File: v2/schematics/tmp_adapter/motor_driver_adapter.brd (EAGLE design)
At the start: 11.8 x 20.2 mm, 2 parts, among them IC1 L293D, IC2 DRV8835

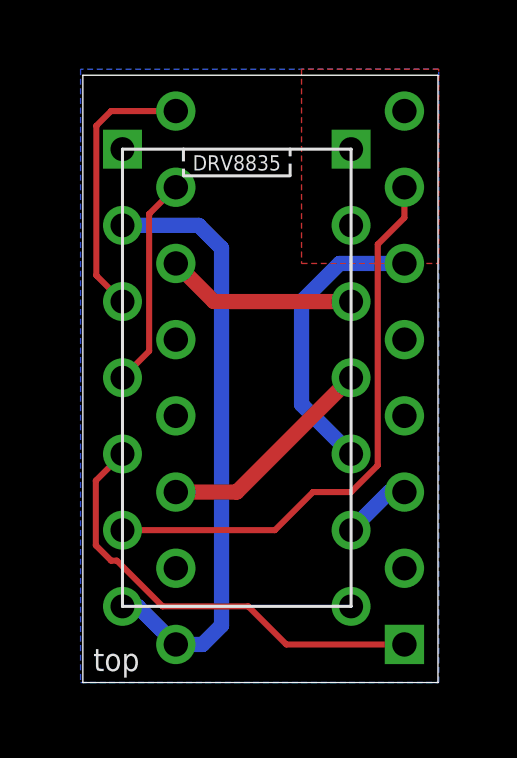
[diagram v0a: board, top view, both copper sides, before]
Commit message: produced prototype version of adapter board
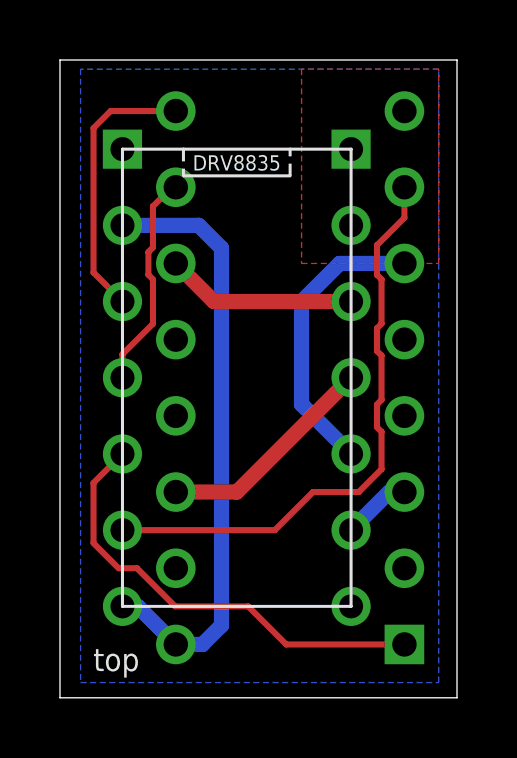
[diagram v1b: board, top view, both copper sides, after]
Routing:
- net MOT_L_DIR: track 19.0 -> 19.6 mm
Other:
- board size 11.8 x 20.2 mm -> 13.2 x 21.3 mm
